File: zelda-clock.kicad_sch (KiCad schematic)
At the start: 11 parts, among them J1 Conn_01x08_Pin, SW1 SW_Push, SW2 SW_Push, SW3 SW_Push, SW4 SW_Push, U1 XIAO-ESP32-C3-SMD

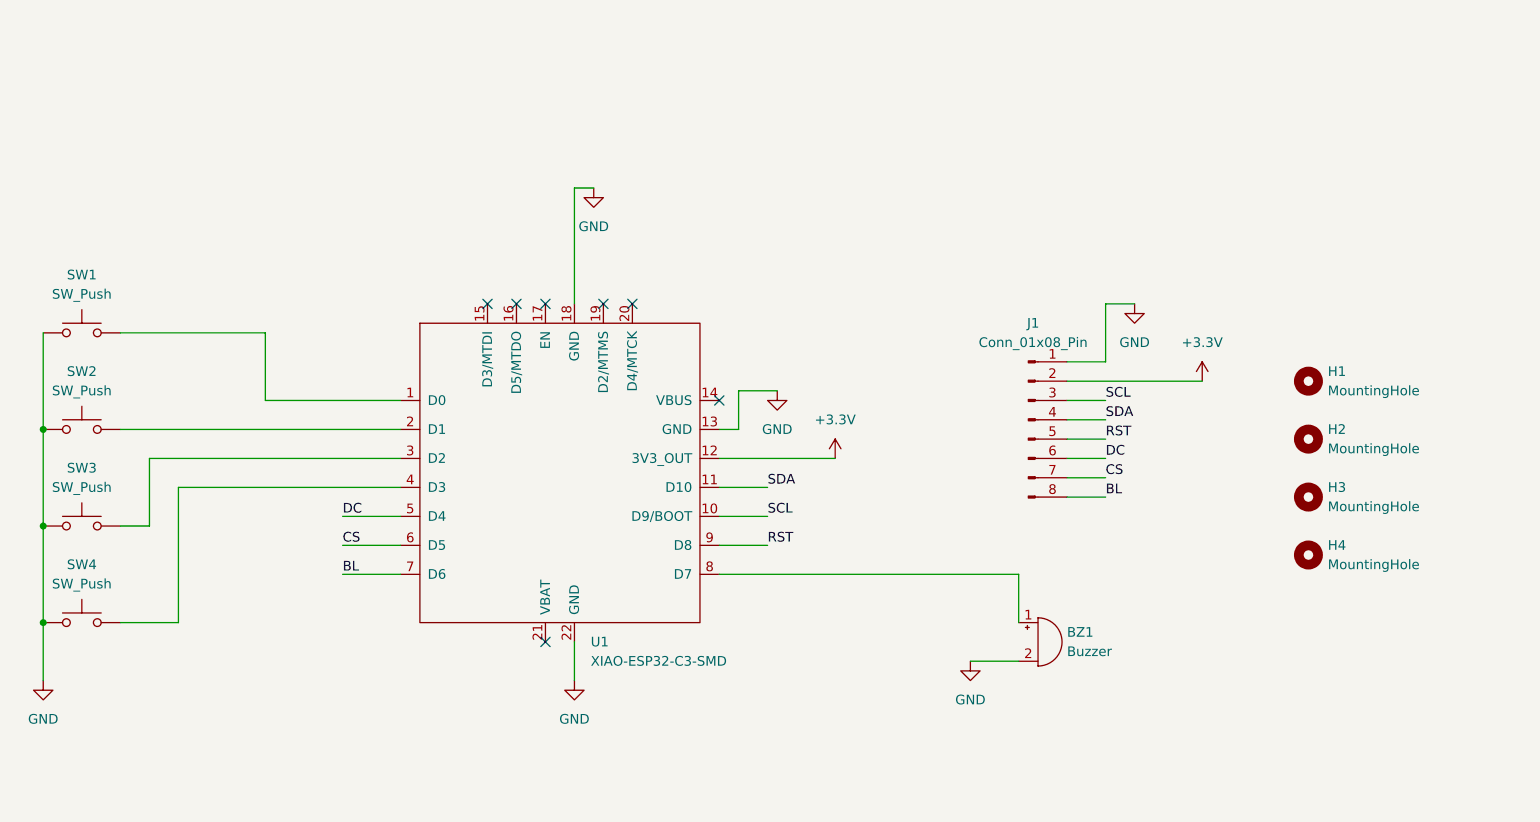
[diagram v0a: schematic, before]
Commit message: update schem
add potentiometer, rgb led and magnetic switch
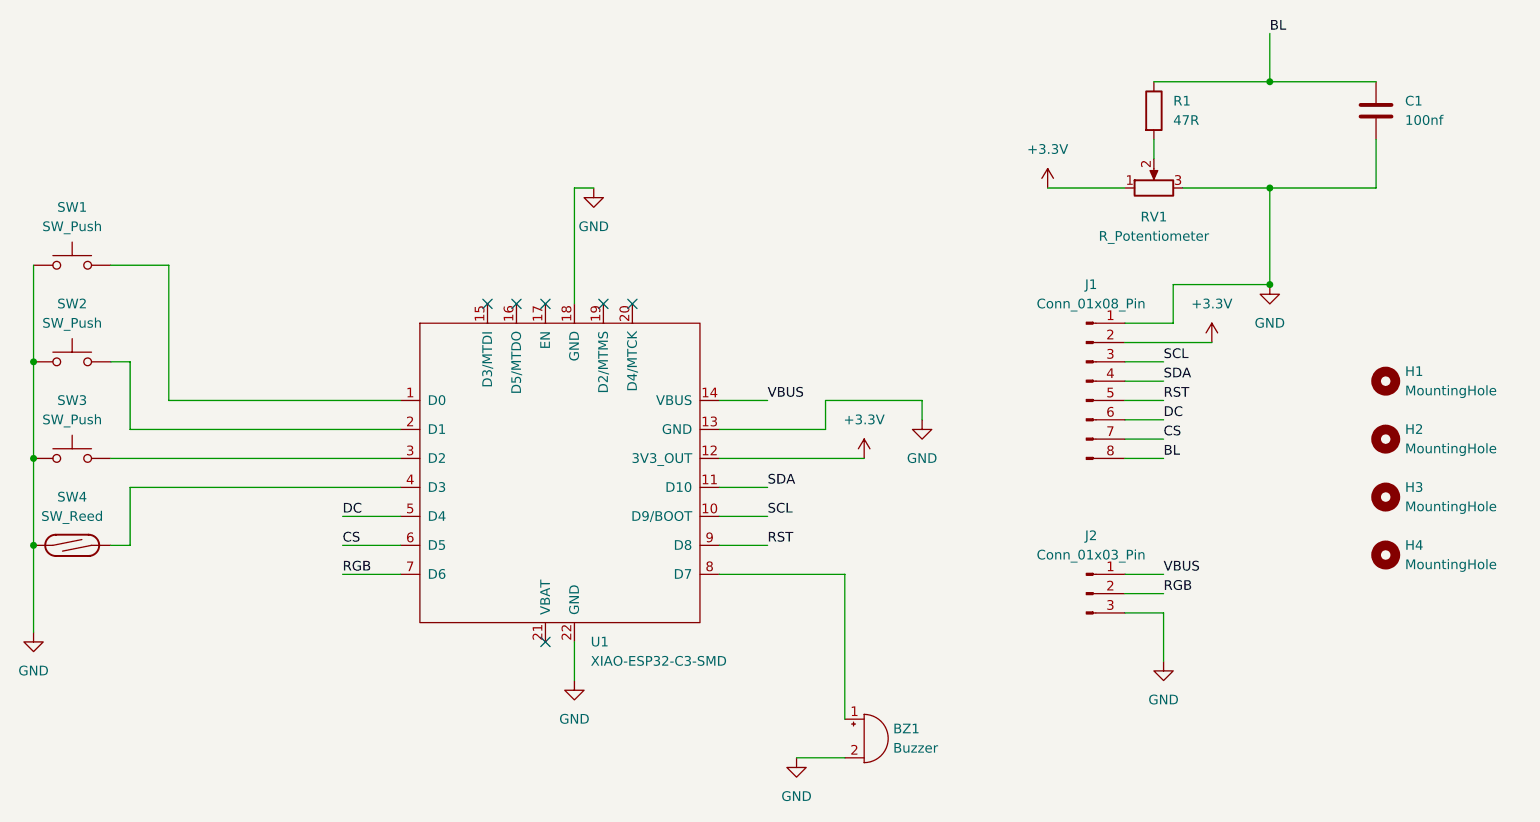
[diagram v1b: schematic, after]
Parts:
- removed SW4: SW_Push, symbol Switch:SW_Push
- added C1: 100nf, Capacitor_THT:C_Disc_D5.0mm_W2.5mm_P2.50mm, symbol Device:C
- added J2: Conn_01x03_Pin, Connector_PinHeader_2.54mm:PinHeader_1x03_P2.54mm_Vertical, symbol Connector:Conn_01x03_Pin
- added R1: 47R, Resistor_THT:R_Axial_DIN0207_L6.3mm_D2.5mm_P7.62mm_Horizontal, symbol Device:R
- added RV1: R_Potentiometer, Potentiometer_THT:Potentiometer_Bourns_3386P_Vertical, symbol Device:R_Potentiometer
- added SW4: SW_Reed, Connector_PinHeader_2.54mm:PinHeader_1x02_P2.54mm_Vertical, symbol Switch:SW_Reed
- BZ1: footprint (none) -> Buzzer_Beeper:Buzzer_12x9.5RM7.6
- H1, H2, H3, H4: footprint (none) -> MountingHole:MountingHole_3.2mm_M3
- J1: footprint (none) -> Connector_PinSocket_2.54mm:PinSocket_1x08_P2.54mm_Vertical
- SW1, SW2, SW3: footprint (none) -> Button_Switch_Keyboard:SW_Cherry_MX_11.00u_PCB
- U1: footprint Seeed_Studio_XIAO_Series:XIAO-ESP32-C3-SMD -> Seeed_Studio_XIAO_Series:XIA0-ESP32-C3-DIP
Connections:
- net +3.3V: now also RV1.1
- net BL: now also C1.2, R1.1; no longer U1.7 (D6)
- net GND: now also C1.1, J2.3 (Pin_3), RV1.3, SW4.1
- net VBUS: now reaches U1.14 (VBUS)
- net VBUS: now also J2.1 (Pin_1)
- net at U1.4 (D3): now also SW4.2
- new net: R1.2, RV1.2
- new net RGB: J2.2 (Pin_2), U1.7 (D6)
- no-connect marks 7 -> 6
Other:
- moved on the sheet: BZ1, H1, H2, H3, H4, J1, SW1, SW2, SW3
